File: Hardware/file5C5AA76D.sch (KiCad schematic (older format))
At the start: 12 parts, among them J14 Conn_01x04_Female, J29 SID_Audio_Connector, U5 MAX7375AXR105, U6 74HC595, U7 74HC595, U8 SID

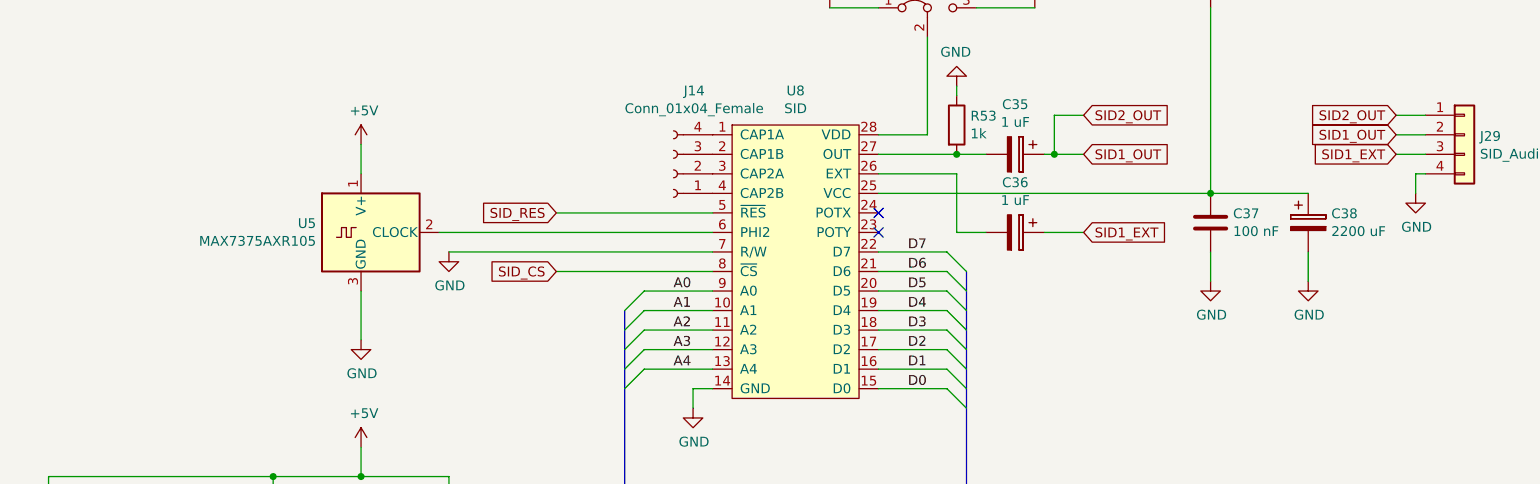
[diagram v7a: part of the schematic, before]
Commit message: Cleaned up some traces, fixes #5
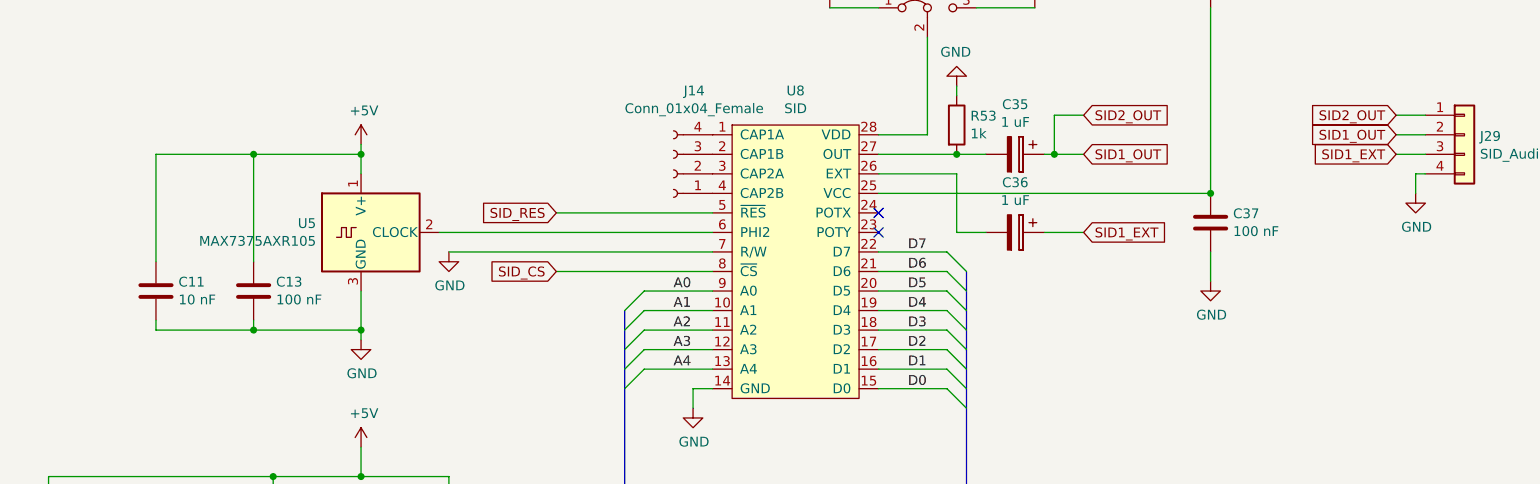
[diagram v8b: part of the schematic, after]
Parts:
- removed C38: 2200 uF, Capacitor_SMD:CP_Elec_10x10, symbol Device:CP
- added C11: 10 nF, Capacitor_SMD:C_0603_1608Metric, symbol Device:C
- added C13: 100 nF, Capacitor_SMD:C_0603_1608Metric, symbol Device:C
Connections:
- net +5V: now also C11.1, C13.1
- net GND: now also C11.2, C13.2
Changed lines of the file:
@@
 	6550 3450 6650 3450
 Wire Wire Line
-	4850 2950 4850 3200
+	4850 2950 4850 3150
 $Comp
 L power:+5V #PWR?
@@
 Wire Wire Line
 	9200 1500 9200 2450
-$Comp
-L Device:CP C38
-U 1 1 5BDEB869
-P 9700 2600
-F 0 "C38" H 9818 2646 50  0000 L CNN
-F 1 "2200 uF" H 9818 2555 50  0000 L CNN
-F 2 "Capacitor_SMD:CP_Elec_10x10" H 9738 2450 50  0001 C CNN
-F 3 "~" H 9700 2600 50  0001 C CNN
-	1    9700 2600
-	1    0    0    -1
-$EndComp
-$Comp
-L power:GND #PWR?
-U 1 1 5BDEB8C2
-P 9700 2900
-AR Path="/5BDEB8C2" Ref="#PWR?"  Part="1"
-AR Path="/5C5AA76E/5BDEB8C2" Ref="#PWR0116"  Part="1"
-F 0 "#PWR0116" H 9700 2650 50  0001 C CNN
-F 1 "GND" H 9705 2727 50  0000 C CNN
-F 2 "" H 9700 2900 50  0001 C CNN
-F 3 "" H 9700 2900 50  0001 C CNN
-	1    9700 2900
-	1    0    0    -1
-$EndComp
-Wire Wire Line
-	9700 2900 9700 2750
-Wire Wire Line
-	9700 2450 9200 2450
 Wire Wire Line
 	5250 2650 6650 2650
@@
 $EndComp
 Wire Wire Line
-	4850 2200 4850 2350
+	4850 2200 4850 2250
+$Comp
+L Device:C C13
+U 1 1 5BFF9FF0
+P 4300 2950
+F 0 "C13" H 4415 2996 50  0000 L CNN
+F 1 "100 nF" H 4415 2905 50  0000 L CNN
+F 2 "Capacitor_SMD:C_0603_1608Metric" H 4338 2800 50  0001 C CNN
+F 3 "~" H 4300 2950 50  0001 C CNN
+	1    4300 2950
+	1    0    0    -1
+$EndComp
+Wire Wire Line
+	4300 3100 4300 3150
+Wire Wire Line
+	4300 3150 4850 3150
+Connection ~ 4850 3150
+Wire Wire Line
+	4850 3150 4850 3200
+Wire Wire Line
+	4300 2800 4300 2250
+Wire Wire Line
+	4300 2250 4850 2250
+Connection ~ 4850 2250
+Wire Wire Line
+	4850 2250 4850 2350
+$Comp
+L Device:C C11
+U 1 1 5C00031F
+P 3800 2950
+F 0 "C11" H 3915 2996 50  0000 L CNN
+F 1 "10 nF" H 3915 2905 50  0000 L CNN
+F 2 "Capacitor_SMD:C_0603_1608Metric" H 3838 2800 50  0001 C CNN
+F 3 "~" H 3800 2950 50  0001 C CNN
+	1    3800 2950
+	1    0    0    -1
+$EndComp
+Wire Wire Line
+	3800 3100 3800 3150
+Wire Wire Line
+	3800 3150 4300 3150
+Connection ~ 4300 3150
+Wire Wire Line
+	3800 2800 3800 2250
+Wire Wire Line
+	3800 2250 4300 2250
+Connection ~ 4300 2250
 Wire Bus Line
 	6200 3050 6200 4050
